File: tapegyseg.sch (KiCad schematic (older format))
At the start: 43 parts

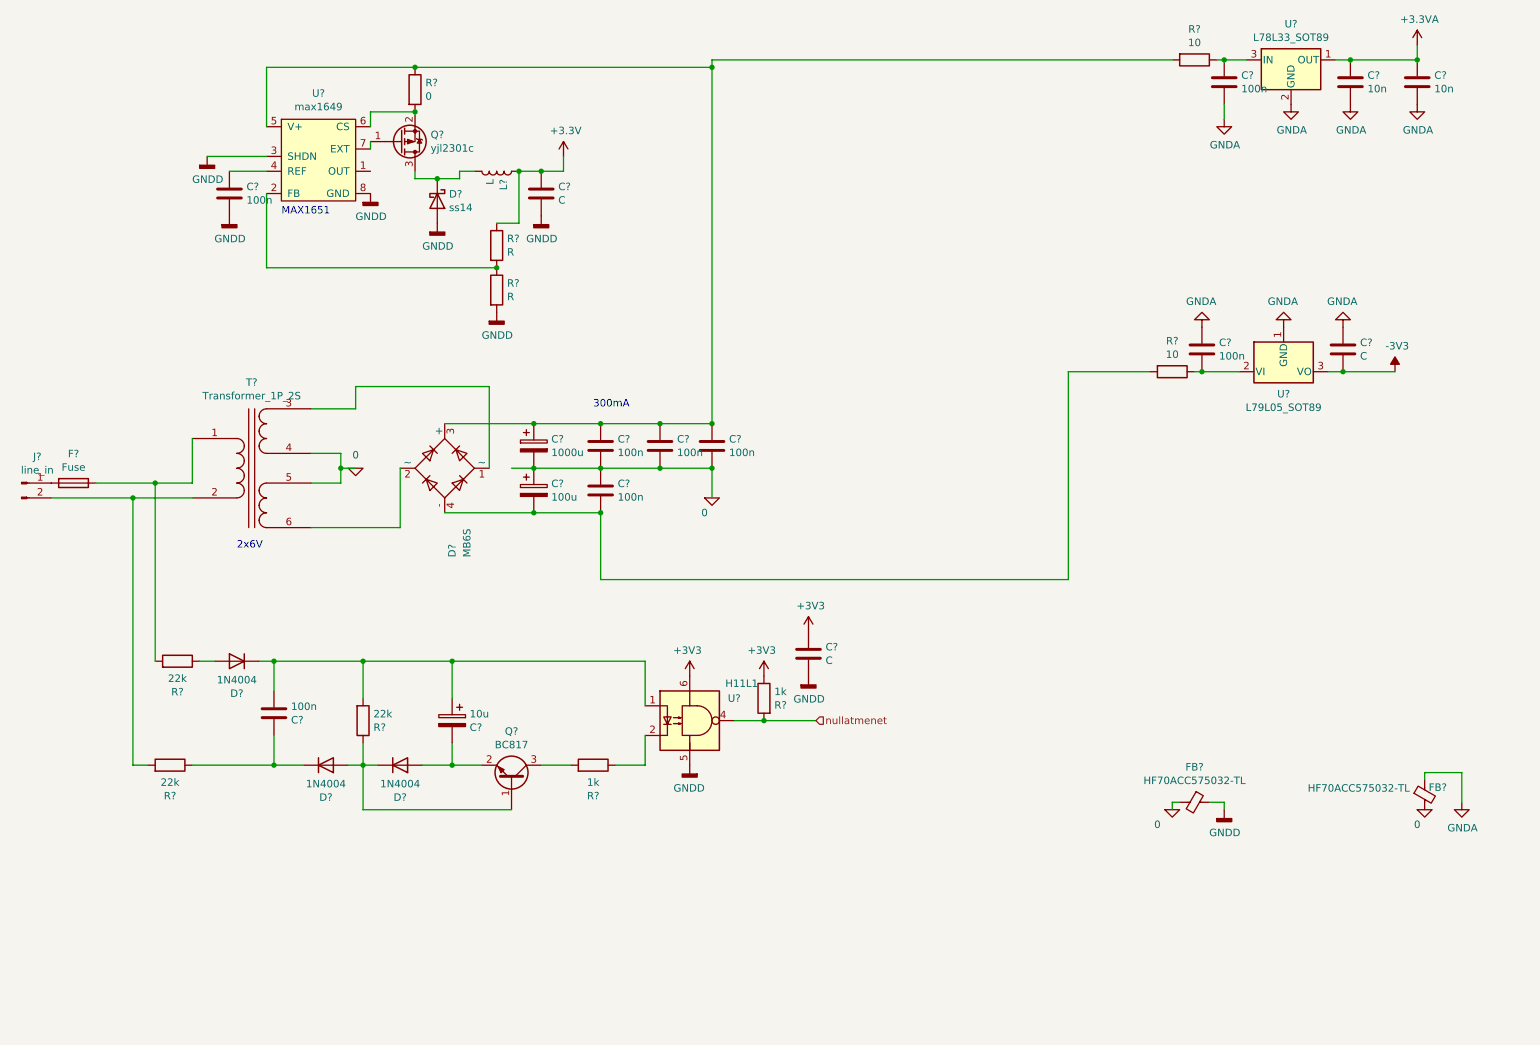
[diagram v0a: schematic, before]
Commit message: Testpoints + ground connections
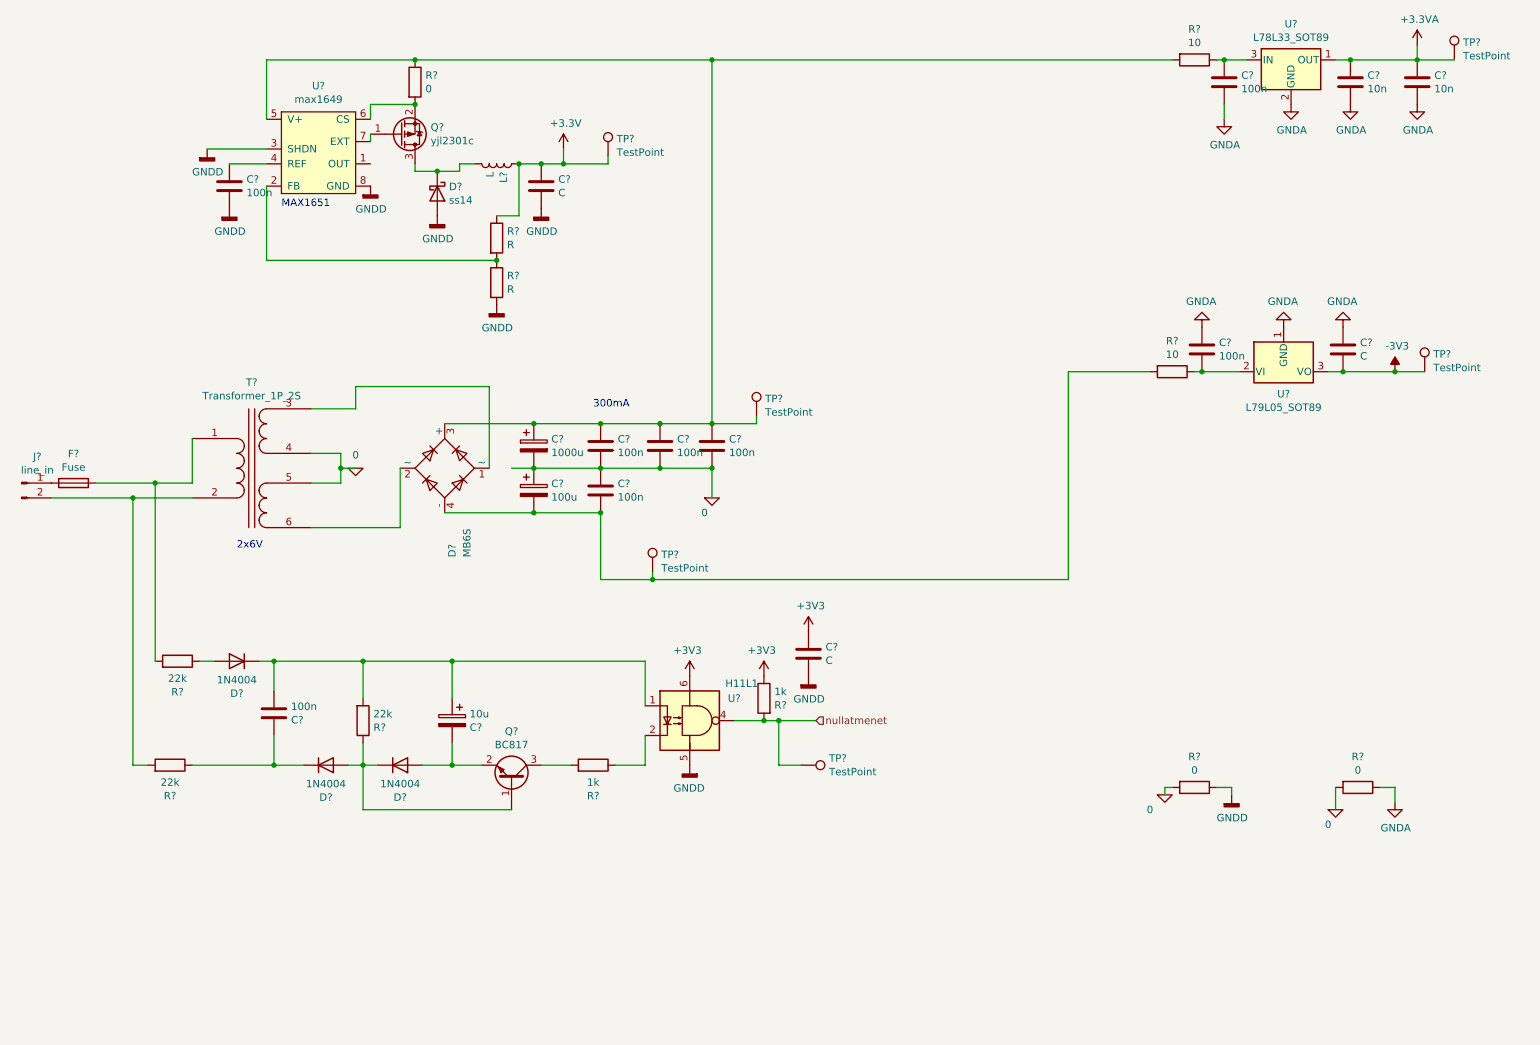
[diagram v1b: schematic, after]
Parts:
- removed FB? (x2): HF70ACC575032-TL, symbol mosogep-rescue:Ferrite_Bead_Small-Device
- added R? (x2): 0, symbol Device:R
- added TP? (x6): TestPoint, symbol Connector:TestPoint
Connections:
- net +3.3VA: now also TP?.1
- net +3V3: now also TP?.1
- net -3V3: now also TP?.1
- net 0: now also R?.2, R?.2
- net GNDA: now also R?.1
- net GNDD: now also R?.1
- net nullatmenet: now also TP?.1
- net at C?.1, C?.1, C?.1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: now also TP?.1
- net at C?.2, C?.2, D?.4 (-)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: now also TP?.1
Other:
- moved on the sheet: C?, D?, L?, Q?, R?, U?

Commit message: ++
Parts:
- removed T?: Transformer_1P_2S, symbol Device:Transformer_1P_2S
- added C55: 10n, Capacitor_SMD:C_0805_2012Metric_Pad1.18x1.45mm_HandSolder, symbol Device:C
- added C58: 47u low esr, Capacitor_THT:CP_Radial_D5.0mm_P2.00mm, symbol mosogep-rescue:CP-Device
- added D19, D20, D21: LED, LED_SMD:LED_0805_2012Metric_Pad1.15x1.40mm_HandSolder, symbol Device:LED
- added R103, R104: R, Resistor_SMD:R_0805_2012Metric_Pad1.20x1.40mm_HandSolder, symbol Device:R
- added R106, R107, R108, R109, R110, R111: 22k/3, Resistor_SMD:R_1206_3216Metric_Pad1.30x1.75mm_HandSolder, symbol Device:R
- added R98: műterhelés, Resistor_SMD:R_1210_3225Metric_Pad1.30x2.65mm_HandSolder, symbol Device:R
- added R99: 330, Resistor_SMD:R_0805_2012Metric_Pad1.20x1.40mm_HandSolder, symbol Device:R
- added TR1: TEZ2.0-D-2, Transformer_THT:Transformer_CHK_EI30-2VA_Neutral, symbol Transformer:TEZ2.0-D-2
- C49, C56, C57, C59, C60, C61, C62, C63, C64, C65, C66: renamed from C?; footprint (none) -> Capacitor_SMD:C_0805_2012Metric_Pad1.18x1.45mm_HandSolder
- C50: renamed from C?; footprint (none) -> Capacitor_THT:C_Rect_L18.0mm_W6.0mm_P15.00mm_FKS3_FKP3
- C51, C52: renamed from C?; footprint (none) -> Capacitor_THT:CP_Radial_D10.0mm_P5.00mm
- C53: renamed from C?; footprint (none) -> Capacitor_THT:CP_Radial_D5.0mm_P2.00mm
- C54: renamed from C?; value C -> 100n; footprint (none) -> Capacitor_SMD:C_0805_2012Metric_Pad1.18x1.45mm_HandSolder
- D14, D15, D16: renamed from D?; value 1N4004 -> do-214AC; footprint Diode_THT:D_DO-41_SOD81_P10.16mm_Horizontal -> Diode_SMD:D_SMA_Handsoldering
- D17: renamed from D?; footprint (none) -> Diode_SMD:D_SMA_Handsoldering
- F1: renamed from F?; footprint (none) -> Fuse:Fuseholder_Cylinder-5x20mm_Schurter_0031_8201_Horizontal_Open
- J7: renamed from J?; footprint (none) -> Connector_Phoenix_GMSTB:PhoenixContact_GMSTBVA_2,5_2-G_1x02_P7.50mm_Vertical
- L2: renamed from L?; value L -> 93-03-18; footprint (none) -> Inductor_SMD:L_Bourns-SRN1060
- Q1: renamed from Q?; footprint (none) -> Package_TO_SOT_SMD:SOT-23W_Handsoldering
- R100, R101, R102, R105, R93, R94, R95, R96, R97: renamed from R?; footprint (none) -> Resistor_SMD:R_0805_2012Metric_Pad1.20x1.40mm_HandSolder
- R90, R91, R92: renamed from R?; value 22k -> 22k/3; footprint (none) -> Resistor_SMD:R_1206_3216Metric_Pad1.30x1.75mm_HandSolder
- TP17, TP18, TP19, TP20, TP21, TP22: renamed from TP?; footprint (none) -> Connector_Pin:Pin_D0.9mm_L10.0mm_W2.4mm_FlatFork
- U12: renamed from U?; footprint (none) -> Package_SO:SOIC-8_3.9x4.9mm_P1.27mm
- U13: renamed from U?; footprint (none) -> Package_DIP:DIP-6_W7.62mm
- U14: renamed from U?; footprint Package_TO_SOT_SMD:SOT-89-3 -> Package_SO:SO-8_3.9x4.9mm_P1.27mm
- gave numbers to parts that had none: 3
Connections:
- net +3.3VA: now also R104.1
- net +3V3: now also C55.1, C58.1, R98.1, R99.1
- net -3V3: now also R103.2
- net 0: now also TR1.7, TR1.9
- net GNDA: now also D20.2 (A), D21.1 (K)
- net GNDD: now also C55.2, C58.2, D19.1 (K), R98.2
- net at F1.1: now also R108.1, TR1.5; no longer R91.2
- net at J7.2 (Pin_2): now also R106.1, TR1.1; no longer R90.2
- net at D18.1 (~~): now also TR1.10
- net at D18.2 (~~): now also TR1.6
- net at C50.1, D15.1 (K): now also R91.1; no longer R90.1
- net at D14.2 (A): now also R90.1; no longer R91.1
- net at C50.2, C51.1, D14.1 (K)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: now also R110.1; no longer R92.2
- new net: R107.2, R90.2
- new net: R109.2, R91.2
- new net: R111.1, R92.2
- new net: D19.2 (A), R99.2
- new net: D20.1 (K), R103.1
- new net: D21.2 (A), R104.2
- new net: R108.2, R109.1
- new net: R106.2, R107.1
- new net: R110.2, R111.2
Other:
- moved on the sheet: R92, TP17

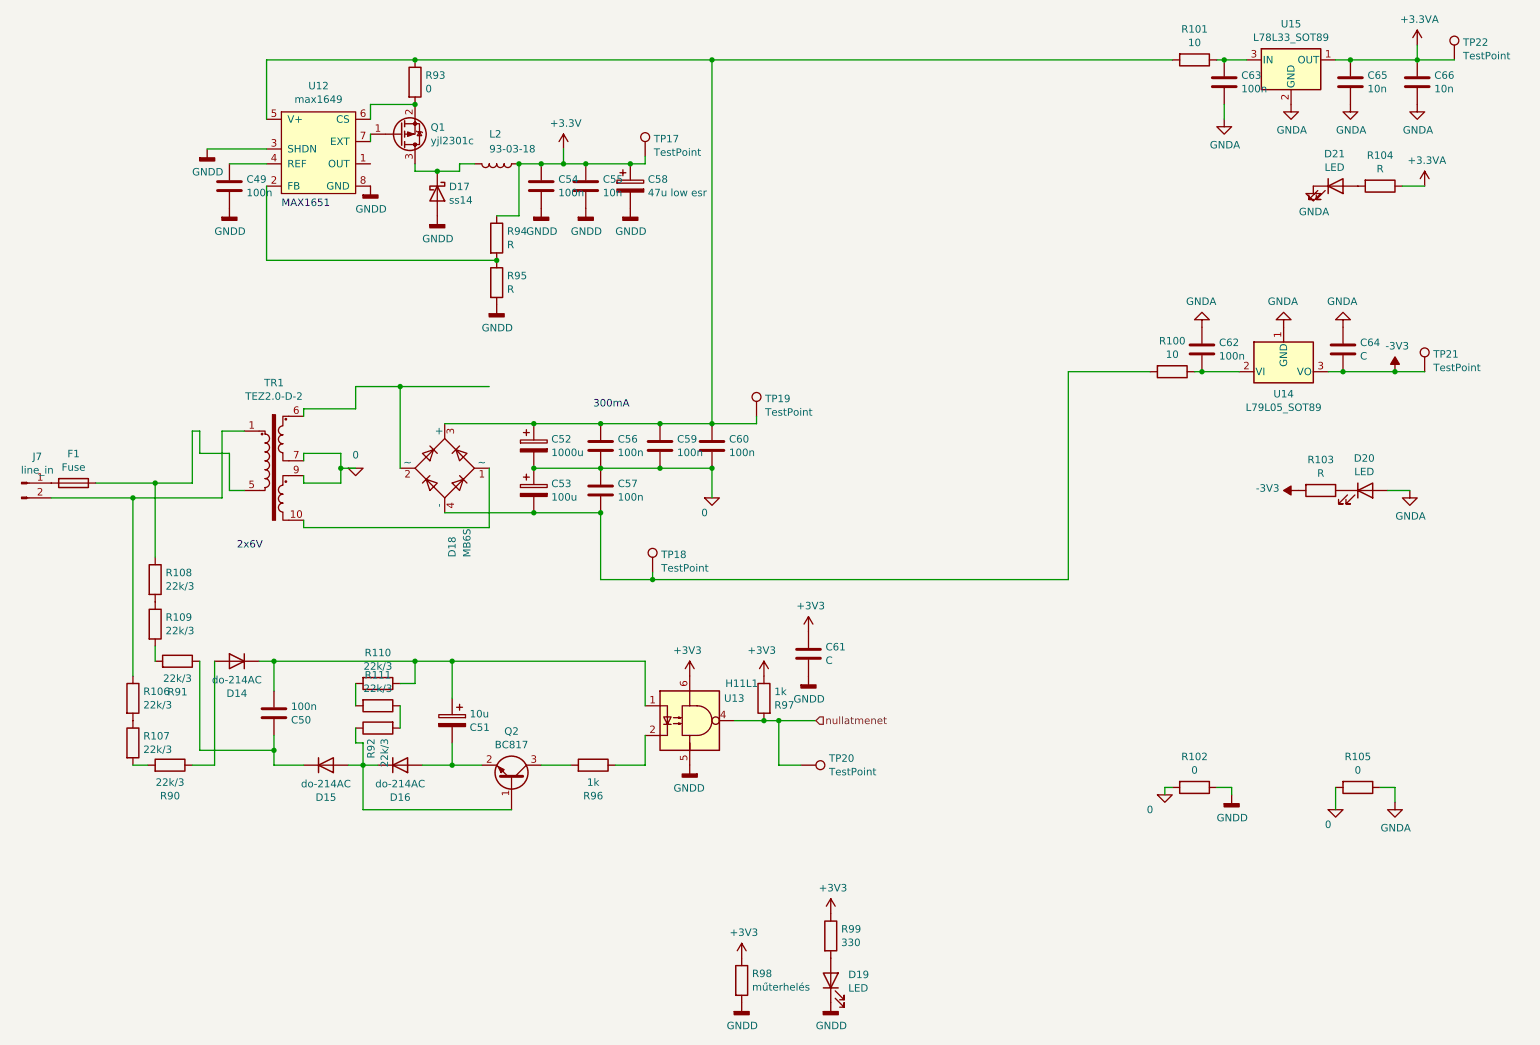
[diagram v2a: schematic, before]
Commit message: Bottom silk
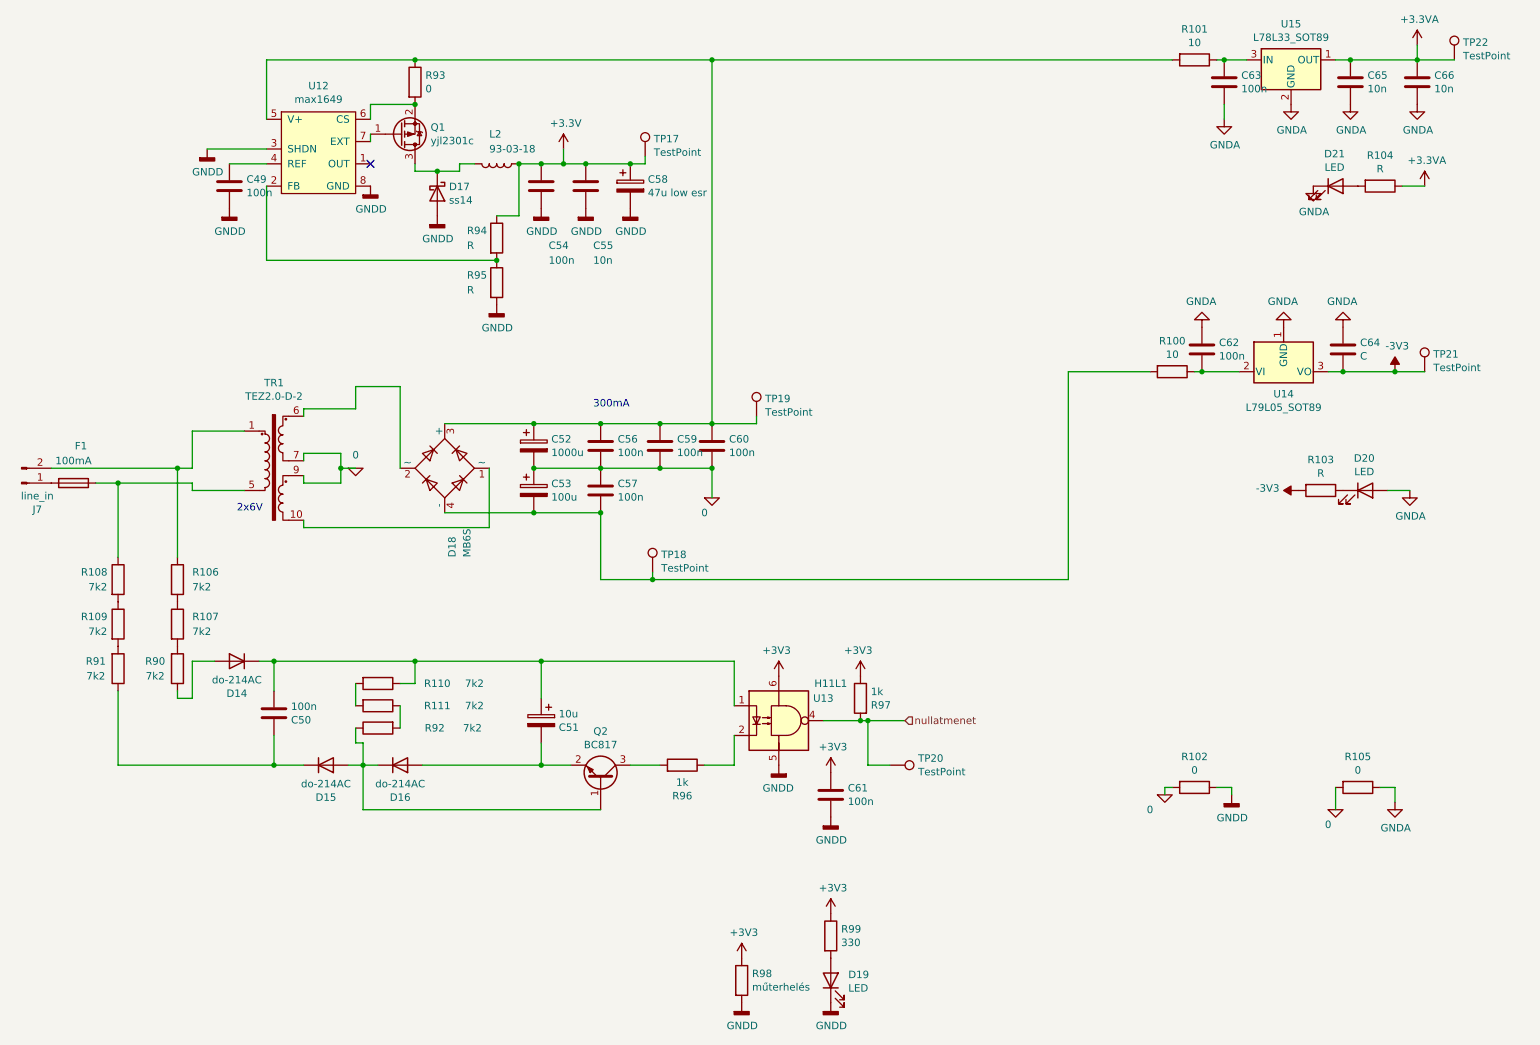
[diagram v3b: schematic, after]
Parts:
- C61: value C -> 100n
- F1: value Fuse -> 100mA
- R106, R107, R108, R109, R110, R111, R90, R91, R92: value 22k/3 -> 7k2
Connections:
- no-connect marks 0 -> 1
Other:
- note removed: "MAX1651"
- moved on the sheet: C51, C61, J7, Q2, R106, R107, R108, R109, R90, R91, R96, R97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
